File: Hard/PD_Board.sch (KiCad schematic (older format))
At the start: 58 parts, among them J1 Micro_SD_Card_Det_Hirose_DM3AT, J2 KRC_Conn_SWD, J3 USB_B_Micro, J4 KRC_Conn_CAN, J5 KRC_Conn_CAN, U1 CY8C58xxLTI-LPxxx, U3 NCV7342, Y1 24MHz

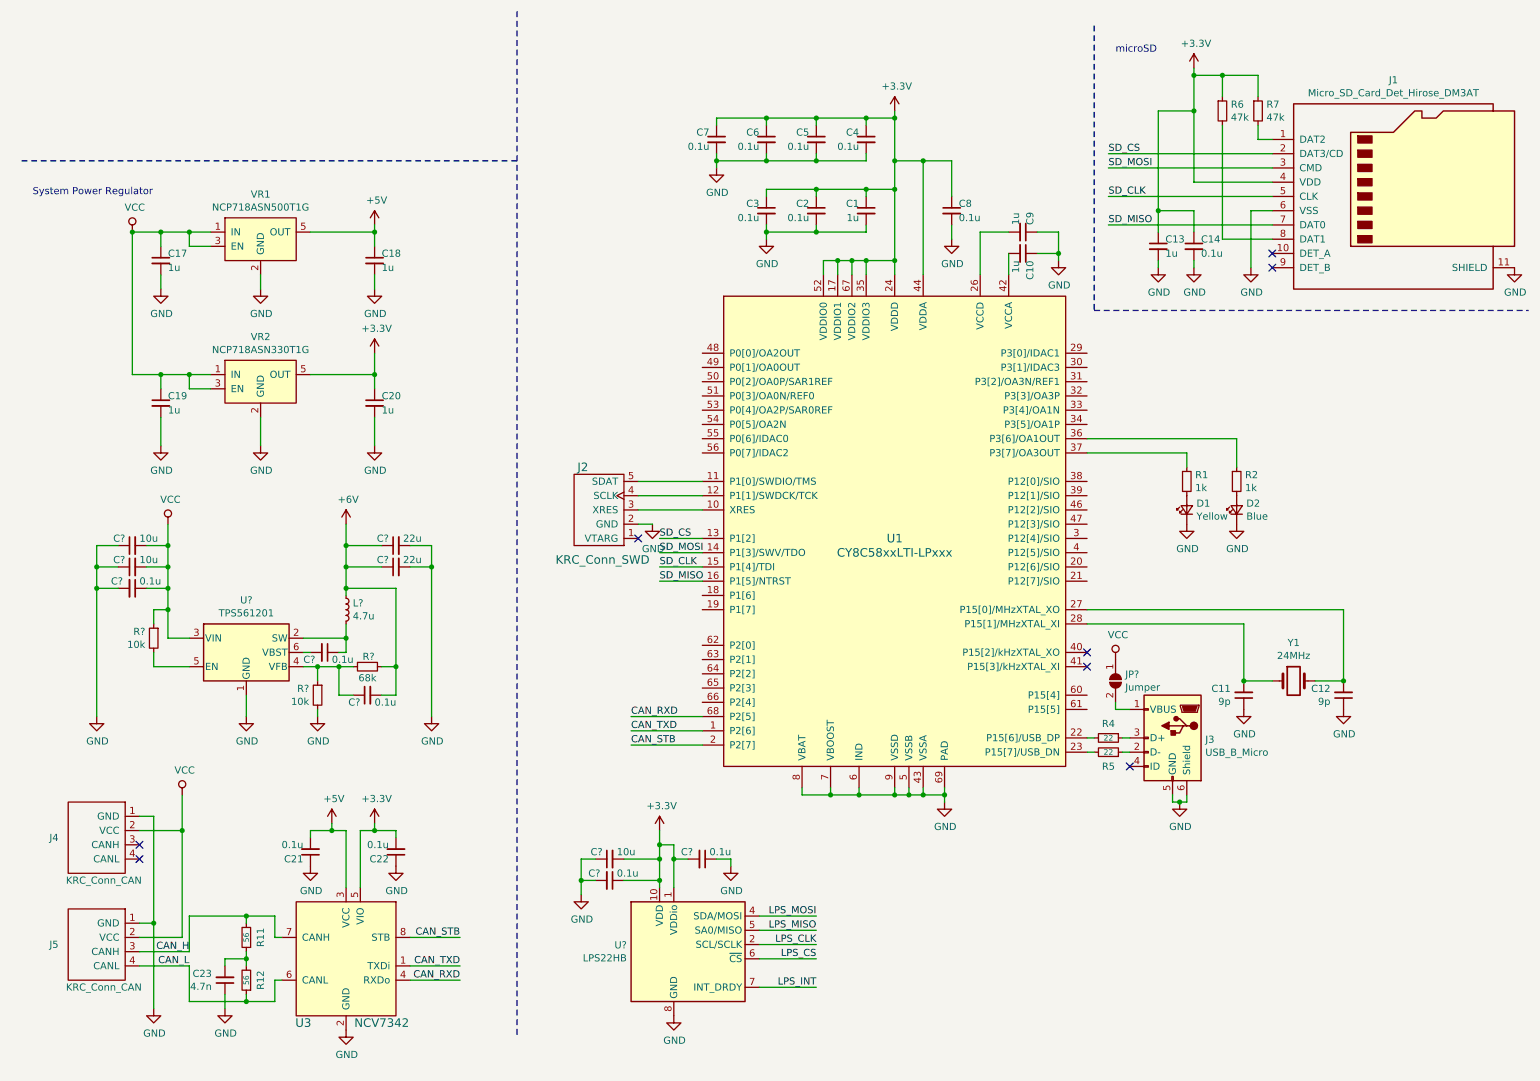
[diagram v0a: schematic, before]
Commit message: [add] 逆流防止用ダイオード追加。回路図仮完成
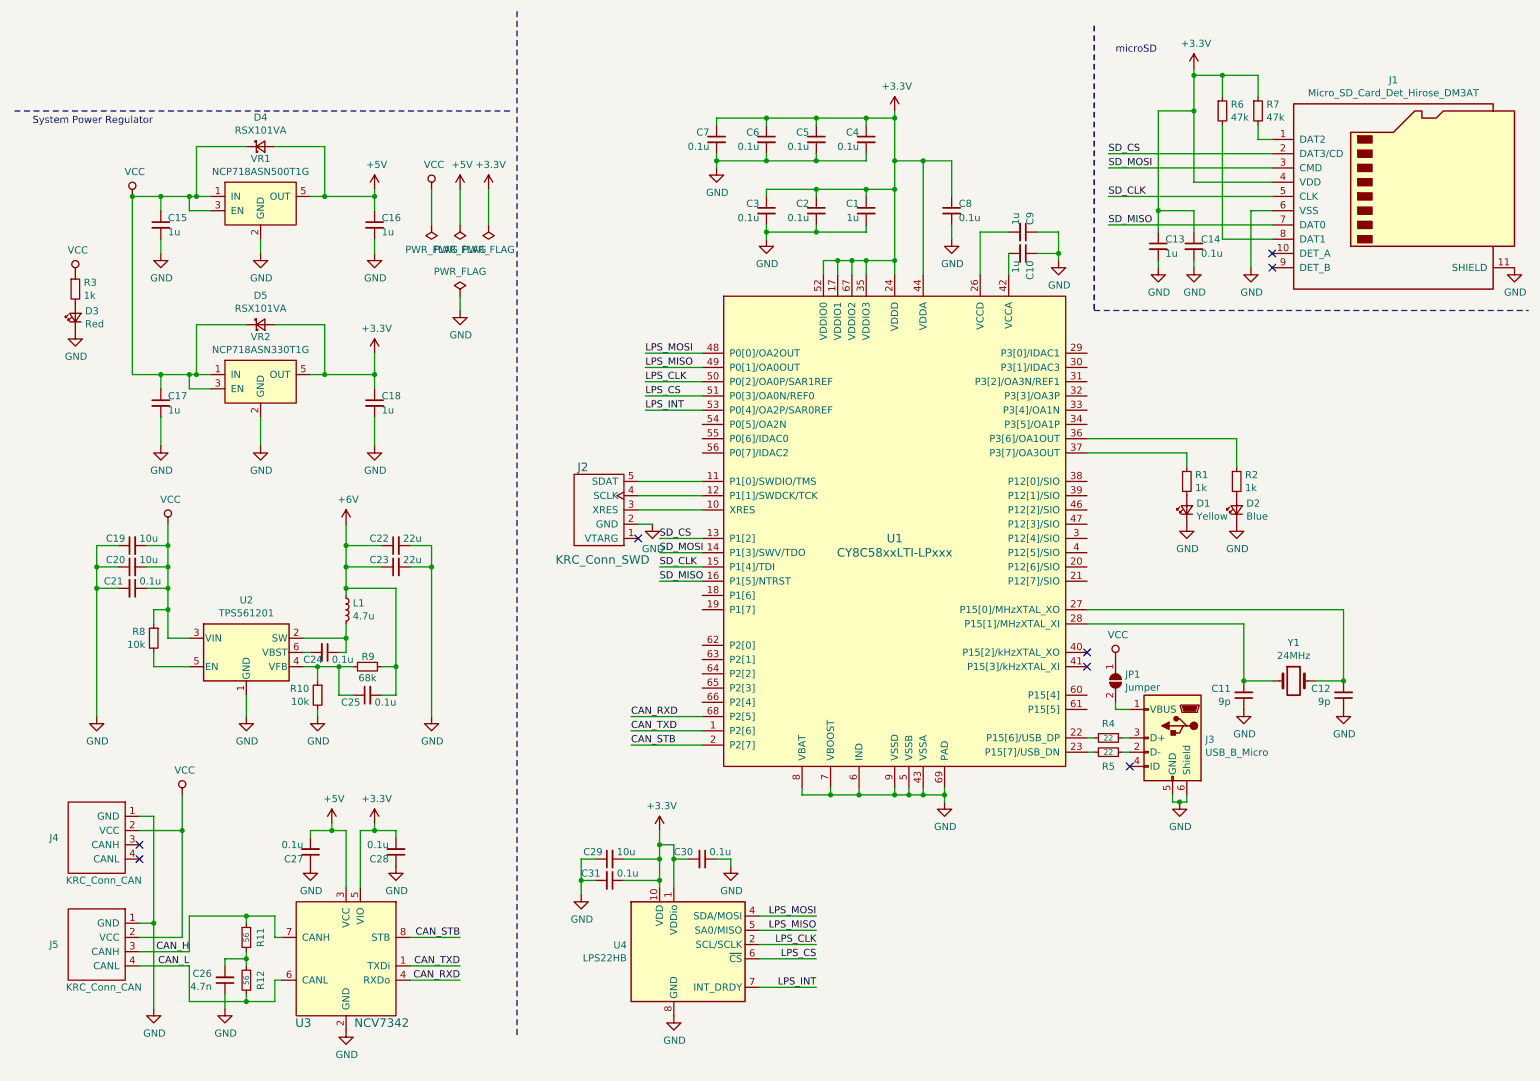
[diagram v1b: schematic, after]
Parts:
- added D3: Red, LED_SMD:LED_0603_1608Metric, symbol Device:LED_Small
- added D4, D5: RSX101VA, Diode_SMD:D_TUMD2, symbol Device:D_Schottky_Small
- added R3: 1k, Resistor_SMD:R_0402_1005Metric, symbol Device:R_Small
- C19, C20, C29: renamed from C?; footprint Capacitor_SMD:C_0402_1005Metric -> Capacitor_SMD:C_0603_1608Metric; Agency Digikey -> 秋月電子; Link https://www.digikey.jp/product-detail/ja/murata-electronics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 -> http://akizukidenshi.com/catalog/g/gP-13161/; MPN GRM155R61E105KA12D -> GRM188R6YA106MA73D; Value 1uF -> 10uF
- JP1: renamed from JP?; footprint (none) -> Jumper:SolderJumper-2_P1.3mm_Open_RoundedPad1.0x1.5mm
- gave numbers to parts that had none: 13
- renumbered C17 to C15, C18 to C16, C19 to C17, C20 to C18, C23 to C26, C21 to C27, C22 to C28
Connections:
- net +3V3: now also D5.2 (A)
- net +5V: now also D4.2 (A)
- net GND: now also D3.1 (K)
- net LPS_CLK: now also U1.50 (P0[2]/OA0P/SAR1REF)
- net LPS_CS: now also U1.51 (P0[3]/OA0N/REF0)
- net LPS_INT: now also U1.53 (P0[4]/OA2P/SAR0REF)
- net LPS_MISO: now also U1.49 (P0[1]/OA0OUT)
- net LPS_MOSI: now also U1.48 (P0[0]/OA2OUT)
- net VCC: now also D4.1 (K), D5.1 (K), R3.1
- new net: D3.2 (A), R3.2
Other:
- moved on the sheet: C15, C16, VR1

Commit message: [add] 配線完了
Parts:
- removed C25: 0.1u, Capacitor_SMD:C_0402_1005Metric, symbol Device:C_Small
- removed J4: KRC_Conn_CAN, Connector_JST:JST_XH_S4B-XH-A_1x04_P2.50mm_Horizontal, symbol KUTKiCad_symbol:KRC_Conn_CAN
- removed JP1: Jumper, Jumper:SolderJumper-2_P1.3mm_Open_RoundedPad1.0x1.5mm, symbol Jumper:SolderJumper_2_Open
- added C31, C32: 1u, Capacitor_SMD:C_0402_1005Metric, symbol Device:C_Small
- added D6: RSX101VA, Diode_SMD:D_TUMD2, symbol Device:D_Schottky_Small
- added J5: Servo, KUTKiCad_footprint:Hirose_DF1E_DF1E-3P-2.5DS_1x03_P2.5mm_Vertical, symbol Connector:Conn_01x03_Male
- added VR3: NCP718ASN330T1G, Package_TO_SOT_SMD:TSOT-23-5, symbol KUTKiCad_symbol:NCP718ASN330T1G
- renumbered C26 to C25, C27 to C26, C28 to C27, C29 to C28, C31 to C29, J5 to J4
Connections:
- net +3V3: now also C32.1, D6.2 (A), VR3.5 (OUT); no longer C13.1, C14.1, C18.1, D5.2 (A), J1.4 (VDD), R6.1, R7.1, VR2.5 (OUT)
- net +6V: now also J5.2 (Pin_2)
- net GND: now also C31.2, C32.2, J5.1 (Pin_1), VR3.2 (GND)
- net LPS_CLK: now also U1.49 (P0[1]/OA0OUT); no longer U1.50 (P0[2]/OA0P/SAR1REF)
- net LPS_MISO: now also U1.50 (P0[2]/OA0P/SAR1REF); no longer U1.49 (P0[1]/OA0OUT)
- net VCC: now also C31.1, D6.1 (K), VR3.1 (IN), VR3.3 (EN)
- net at R1.1: now also U1.4 (P12[5]/SIO); no longer U1.37 (P3[7]/OA3OUT)
- net at U1.3 (P12[4]/SIO): now also R2.1
- net Servo: now reaches U1.34 (P3[5]/OA1P)
- net Servo: now also J5.3 (Pin_3)
- net at U1.36 (P3[6]/OA1OUT): no longer R2.1
- new net +3.3VP: C13.1, C14.1, C18.1, D5.2 (A), J1.4 (VDD), R6.1, R7.1, VR2.5 (OUT)
- no-connect marks 8 -> 32
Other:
- moved on the sheet: C15, C16, C17, C18, C19, C20, C21, C22, C23, C24, C25, C26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

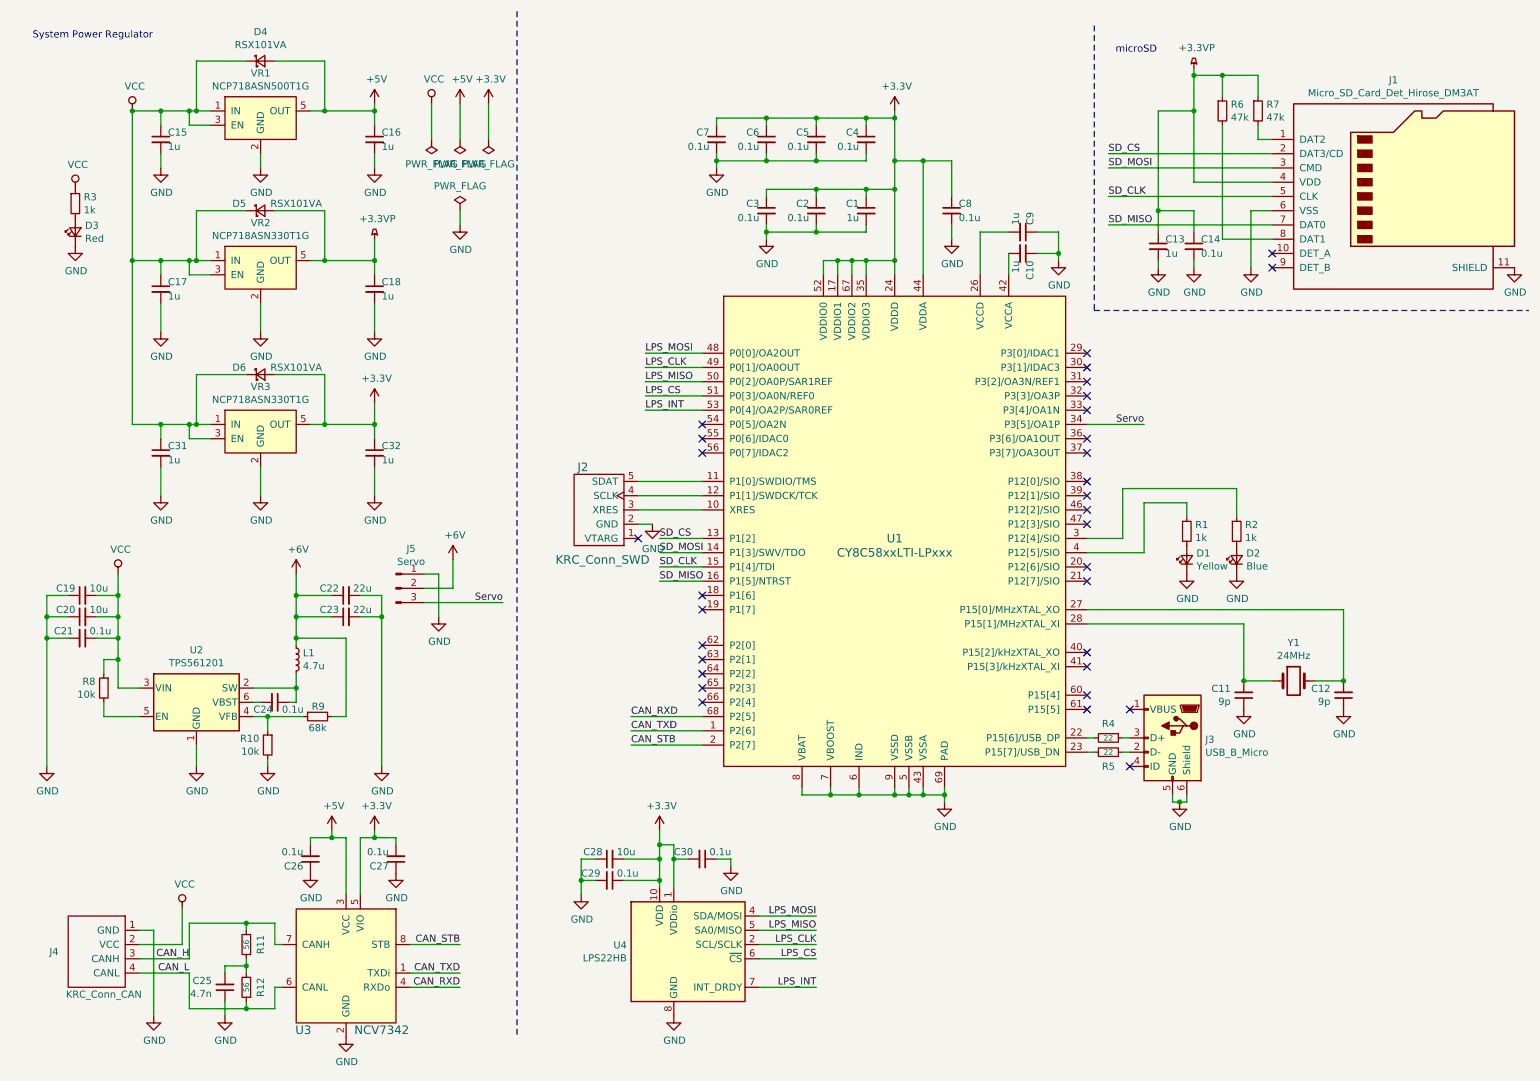
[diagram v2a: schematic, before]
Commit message: [update] プルアップ抵抗ちゃんとしました
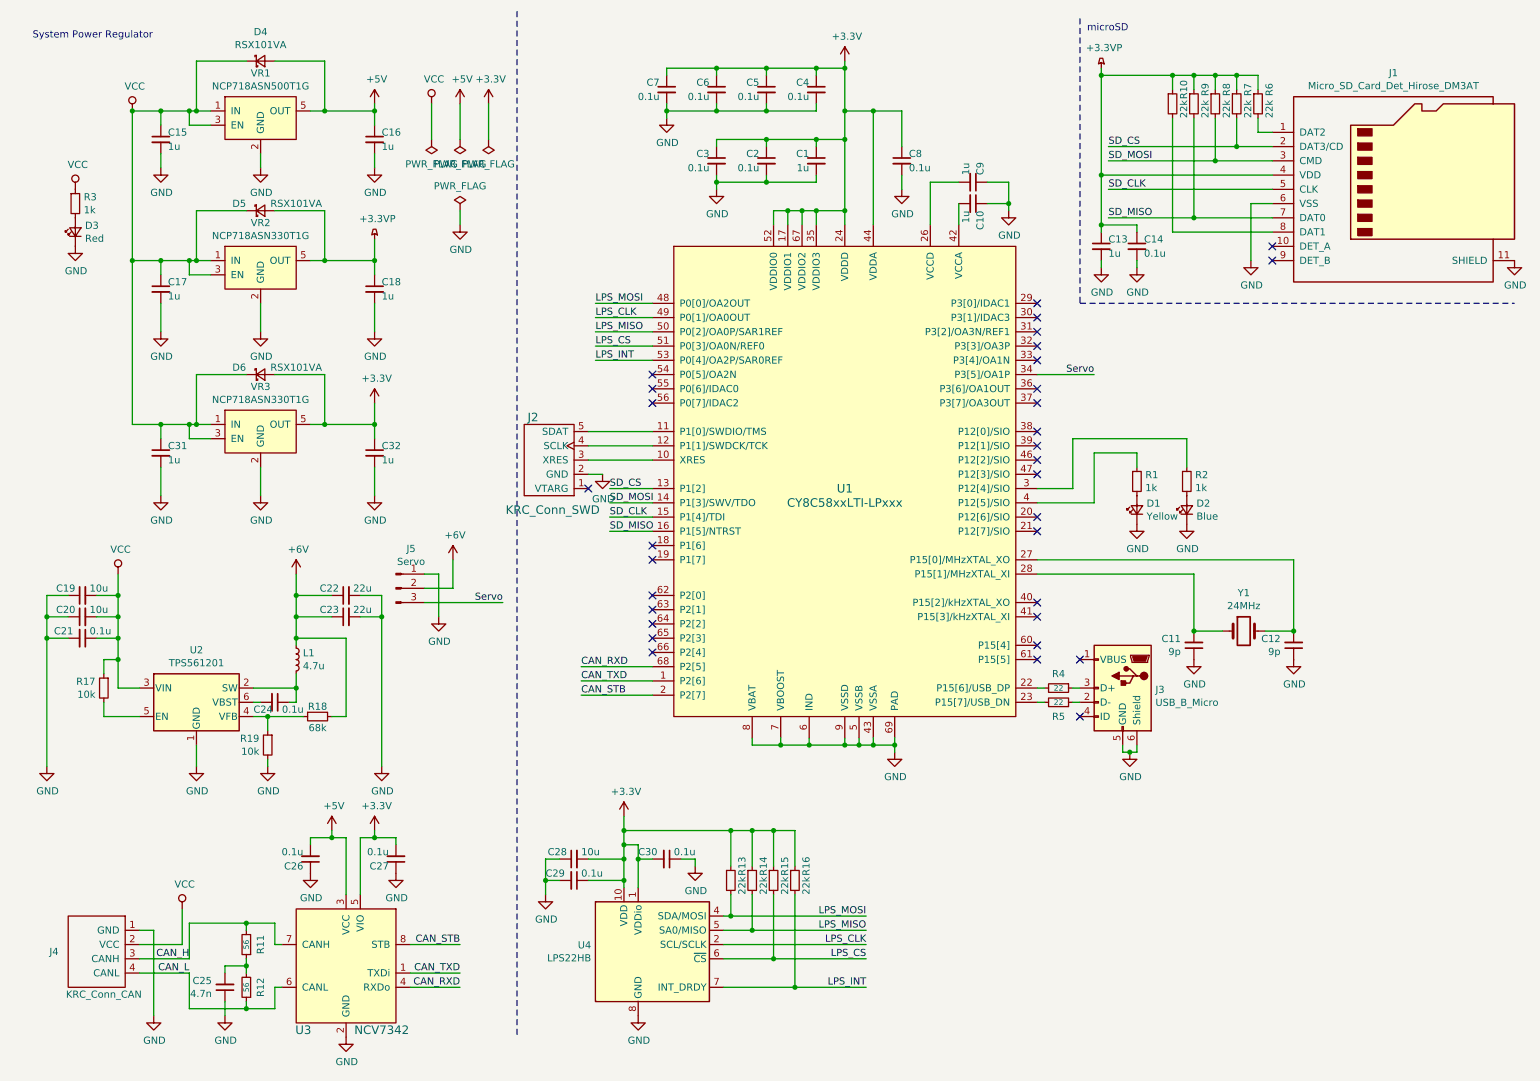
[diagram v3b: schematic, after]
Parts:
- added R10, R13, R14, R15, R16, R8, R9: 22k, Resistor_SMD:R_0402_1005Metric, symbol Device:R_Small
- R6, R7: value 47k -> 22k; Link https://www.digikey.jp/product-detail/ja/panasonic-electronic-components/ERJ-2GEJ473X/P47KJCT-ND/147021 -> https://www.digikey.jp/product-detail/ja/panasonic-electronic-components/ERJ-2RKF2202X/P22.0KLCT-ND/1746653; MPN ERJ-2GEJ473X -> ERJ-2RKF2202X; Value 47kΩ -> 22kΩ
- renumbered R8 to R17, R9 to R18, R10 to R19
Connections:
- net +3.3VP: now also R10.1, R8.1, R9.1
- net +3V3: now also R13.1, R14.1, R15.1, R16.1
- net LPS_CS: now also R15.2
- net LPS_INT: now also R16.2
- net LPS_MISO: now also R14.2
- net LPS_MOSI: now also R13.2
- net SD_CS: now also R7.2
- net SD_MISO: now also R9.2
- net SD_MOSI: now also R8.2
- net at J1.1 (DAT2): now also R6.2; no longer R7.2
- net at J1.8 (DAT1): now also R10.2; no longer R6.2
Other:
- moved on the sheet: C1, C10, C11, C12, C13, C14, C2, C28, C29, C3, C30, C4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

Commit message: [update] READMEを整備
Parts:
- C19, C20, C28, D4, D5, D6, J1: Agency 秋月電子 -> akizuki
- U4: Agency (none) -> Digikey; Link (none) -> https://www.digikey.jp/product-detail/ja/stmicroelectronics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; MPN (none) -> LPS22HBTR
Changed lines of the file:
@@
 F 2 "Connector_Card:microSD_HC_Hirose_DM3AT-SF-PEJM5" H 12300 2350 50  0001 C CNN
 F 3 "https://www.hirose.com/product/en/download_file/key_name/DM3/category/Catalog/doc_file_id/49662/?file_category_id=4&item_id=195&is_series=1" H 10250 1750 50  0001 C CNN
-F 4 "秋月電子" H 10250 1650 50  0001 C CNN "Agency"
+F 4 "akizuki" H 10250 1650 50  0001 C CNN "Agency"
 F 5 "DM3AT-SF-PEJM5" H 10250 1650 50  0001 C CNN "MPN"
 F 6 "http://akizukidenshi.com/catalog/g/gC-02395/" H 10250 1650 50  0001 C CNN "Link"
@@
 F 2 "Capacitor_SMD:C_0603_1608Metric" H 1000 4500 50  0001 C CNN
 F 3 "https://search.murata.co.jp/Ceramy/image/img/A01X/G101/ENG/GRM188R6YA106MA73-01.pdf" H 1000 4500 50  0001 C CNN
-F 4 "秋月電子" H 1000 4500 50  0001 C CNN "Agency"
+F 4 "akizuki" H 1000 4500 50  0001 C CNN "Agency"
 F 5 "GRM188R6YA106MA73D" H 1000 4500 50  0001 C CNN "MPN"
 F 6 "10uF" H 1000 4500 50  0001 C CNN "Value"
@@
 F 2 "Capacitor_SMD:C_0603_1608Metric" H 1000 4650 50  0001 C CNN
 F 3 "https://search.murata.co.jp/Ceramy/image/img/A01X/G101/ENG/GRM188R6YA106MA73-01.pdf" H 1000 4650 50  0001 C CNN
-F 4 "秋月電子" H 1000 4650 50  0001 C CNN "Agency"
+F 4 "akizuki" H 1000 4650 50  0001 C CNN "Agency"
 F 5 "GRM188R6YA106MA73D" H 1000 4650 50  0001 C CNN "MPN"
 F 6 "10uF" H 1000 4650 50  0001 C CNN "Value"
@@
 F 2 "Package_LGA:ST_HLGA-10_2.5x2.5mm_P0.6mm_LayoutBorder3x2y" H 5000 6750 50  0001 C CNN
 F 3 "www.st.com/resource/en/datasheet/lps25hb.pdf" H 5050 6600 50  0001 C CNN
+F 4 "Digikey" H 0   0   50  0001 C CNN "Agency"
+F 5 "https://www.digikey.jp/product-detail/ja/stmicroelectronics/LPS22HBTR/497-16265-1-ND/5799917" H 0   0   50  0001 C CNN "Link"
+F 6 "LPS22HBTR" H 0   0   50  0001 C CNN "MPN"
 	1    5000 6950
 	1    0    0    -1
@@
 F 2 "Capacitor_SMD:C_0603_1608Metric" H 4450 6350 50  0001 C CNN
 F 3 "https://search.murata.co.jp/Ceramy/image/img/A01X/G101/ENG/GRM188R6YA106MA73-01.pdf" H 4450 6350 50  0001 C CNN
-F 4 "秋月電子" H 4450 6350 50  0001 C CNN "Agency"
+F 4 "akizuki" H 4450 6350 50  0001 C CNN "Agency"
 F 5 "GRM188R6YA106MA73D" H 4450 6350 50  0001 C CNN "MPN"
 F 6 "10uF" H 4450 6350 50  0001 C CNN "Value"
@@
 F 2 "Diode_SMD:D_TUMD2" V 2250 750 50  0001 C CNN
 F 3 "http://akizukidenshi.com/download/ds/rohm/rsx101vam30-j.pdf" V 2250 750 50  0001 C CNN
-F 4 "秋月電子" H 2250 750 50  0001 C CNN "Agency"
+F 4 "akizuki" H 2250 750 50  0001 C CNN "Agency"
 F 5 "http://akizukidenshi.com/catalog/g/gI-05951/" H 2250 750 50  0001 C CNN "Link"
 F 6 "RSX101VAM-30TR" H 2250 750 50  0001 C CNN "MPN"
@@
 F 2 "Diode_SMD:D_TUMD2" V 2250 1800 50  0001 C CNN
 F 3 "http://akizukidenshi.com/download/ds/rohm/rsx101vam30-j.pdf" V 2250 1800 50  0001 C CNN
-F 4 "秋月電子" H 2250 1800 50  0001 C CNN "Agency"
+F 4 "akizuki" H 2250 1800 50  0001 C CNN "Agency"
 F 5 "http://akizukidenshi.com/catalog/g/gI-05951/" H 2250 1800 50  0001 C CNN "Link"
 F 6 "RSX101VAM-30TR" H 2250 1800 50  0001 C CNN "MPN"
@@
 F 2 "Diode_SMD:D_TUMD2" V 2250 2950 50  0001 C CNN
 F 3 "http://akizukidenshi.com/download/ds/rohm/rsx101vam30-j.pdf" V 2250 2950 50  0001 C CNN
-F 4 "秋月電子" H 2250 2950 50  0001 C CNN "Agency"
+F 4 "akizuki" H 2250 2950 50  0001 C CNN "Agency"
 F 5 "http://akizukidenshi.com/catalog/g/gI-05951/" H 2250 2950 50  0001 C CNN "Link"
 F 6 "RSX101VAM-30TR" H 2250 2950 50  0001 C CNN "MPN"
